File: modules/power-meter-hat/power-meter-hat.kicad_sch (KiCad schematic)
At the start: 17 parts, among them J1 GPIO, J2 Barrel_Jack_Switch, U1 CAT24C256, U2 NCP1117-3.3_SOT223

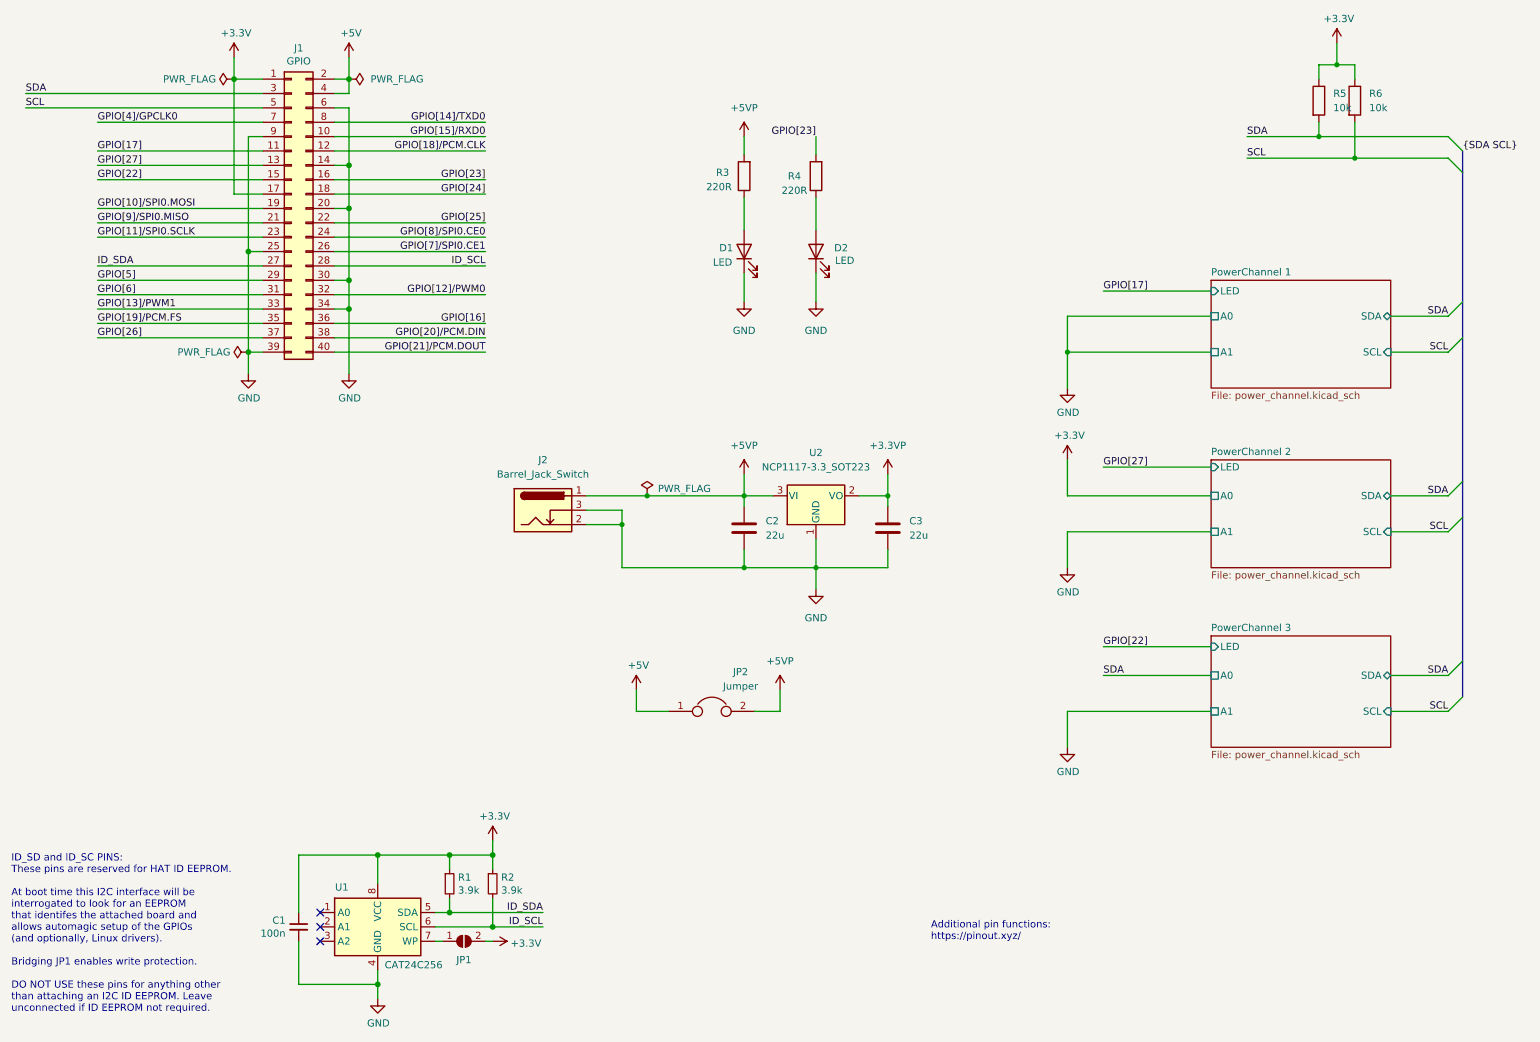
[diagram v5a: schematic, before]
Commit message: Add test points for SDA/SCL/GND
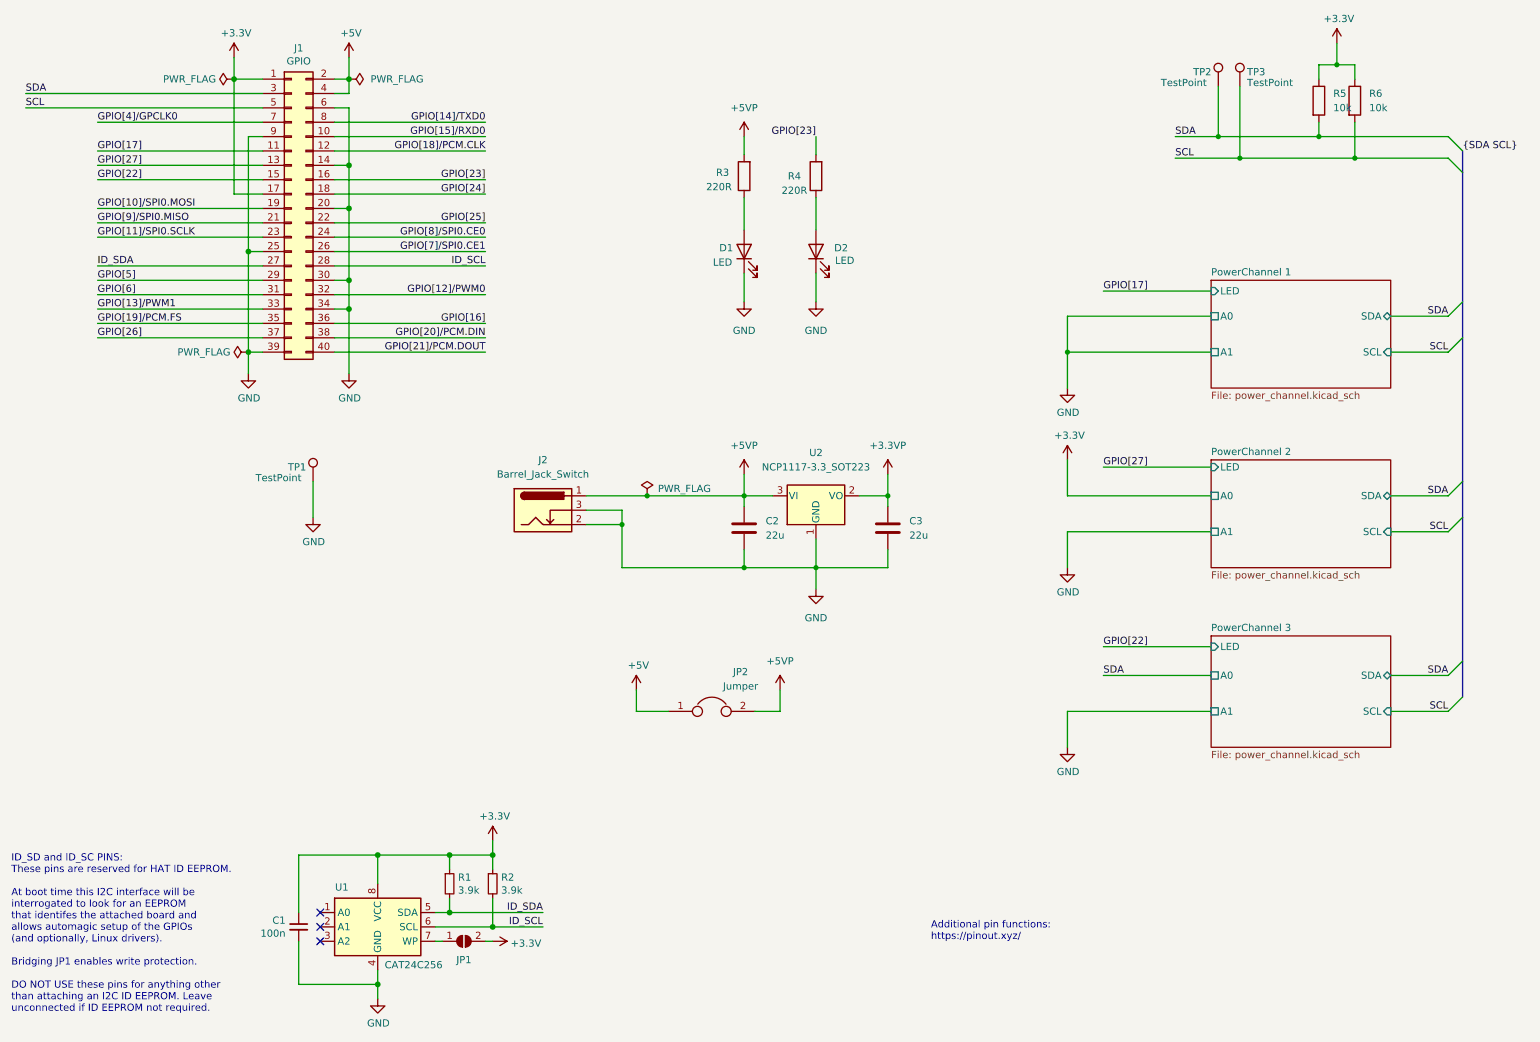
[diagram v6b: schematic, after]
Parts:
- added TP1, TP2, TP3: TestPoint, TestPoint:TestPoint_Loop_D2.54mm_Drill1.5mm_Beaded, symbol Connector:TestPoint
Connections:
- net GND: now also TP1.1
- net SCL: now also TP3.1
- net SDA: now also TP2.1

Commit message: Update components and footprints
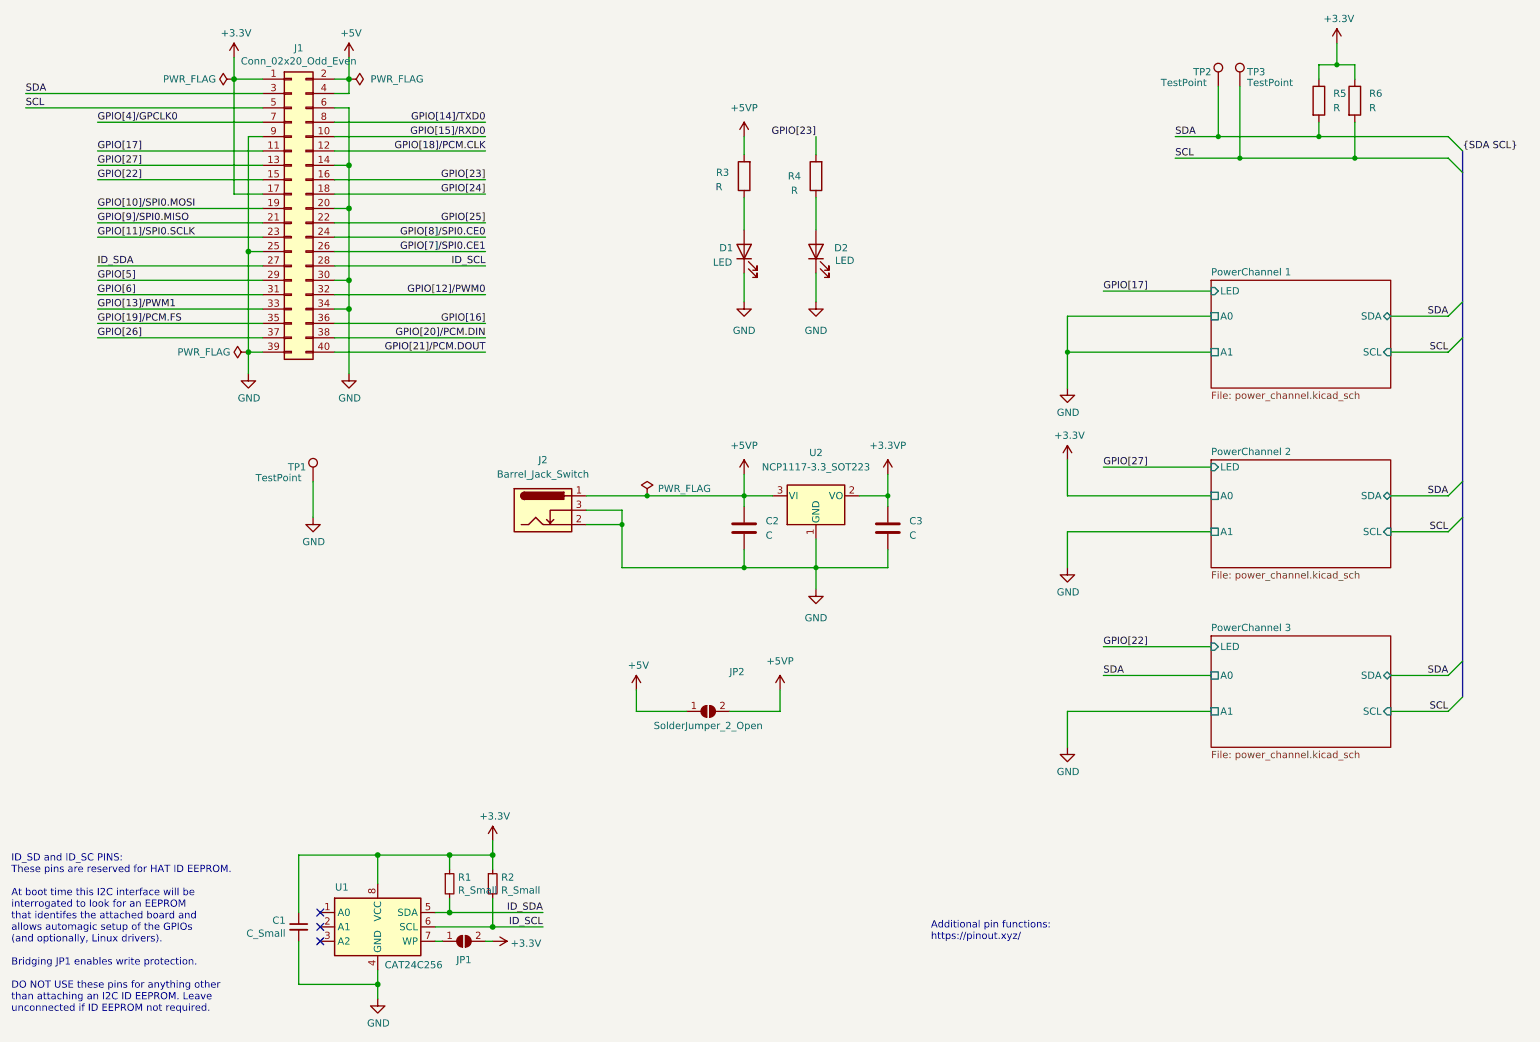
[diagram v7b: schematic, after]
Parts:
- C1: value 100n -> C_Small
- C2, C3: value 22u -> C
- D1, D2: footprint LED_SMD:LED_1206_3216Metric_Castellated -> LED_SMD:LED_1206_3216Metric
- J1: value GPIO -> Conn_02x20_Odd_Even
- JP1: value ID_WP -> SolderJumper_2_Open
- JP2: value Jumper -> SolderJumper_2_Open; symbol Device:Jumper -> Jumper:SolderJumper_2_Open
- R1, R2: value 3.9k -> R_Small
- R3, R4: value 220R -> R
- R5, R6: value 10k -> R
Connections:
- net +3V3 renamed +3.3V

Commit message: Add "ideal diode" and fuse, update values
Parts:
- added F1: MF-MSMF250/16X-2, Fuse:Fuse_1812_4532Metric_Castellated, symbol Device:Polyfuse_Small
- added Q1: BC856BDW1, Package_TO_SOT_SMD:SOT-363_SC-70-6, symbol Transistor_BJT:BC856BDW1
- added Q2: SI2301CDS, Package_TO_SOT_SMD:SOT-23, symbol shared_components:P-Channel_MOSFET,_SOT-23
- added R1: 10k, Resistor_SMD:R_0805_2012Metric_Pad1.20x1.40mm_HandSolder, symbol Device:R_Small
- added R2: 47k, Resistor_SMD:R_0805_2012Metric_Pad1.20x1.40mm_HandSolder, symbol Device:R_Small
- C1: value C_Small -> 100n
- C2, C3: value C -> 22u
- J2: renamed from J1; value Conn_02x20_Odd_Even -> GPIO
- JP1: value SolderJumper_2_Open -> ID_WP
- JP2: value SolderJumper_2_Open -> 5V_Bridge
- R3: renamed from R1; value R_Small -> 3.9k
- R4: renamed from R2; value R_Small -> 3.9k
- R5: renamed from R3; value R -> 220R
- R6: renamed from R4; value R -> 220R
- R7: renamed from R5; value R -> 10k
- R8: renamed from R6; value R -> 10k
- renumbered J2 to J1
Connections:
- net +5VP: now also Q1.1 (E1), Q2.2 (S); no longer J1.1
- net GND: now also R1.2, R2.2
- new net: Q1.2 (B1), Q1.3 (C2), Q1.5 (B2), R1.1
- new net: Q1.6 (C1), Q2.1 (G), R2.1
- new net Vfused: F1.2, Q1.4 (E2), Q2.3 (D)
- new net Vpsu: F1.1, J1.1
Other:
- moved on the sheet: J1, JP2, TP1
